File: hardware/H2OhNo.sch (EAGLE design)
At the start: 12 parts, among them U2 TINY85-20-DIP

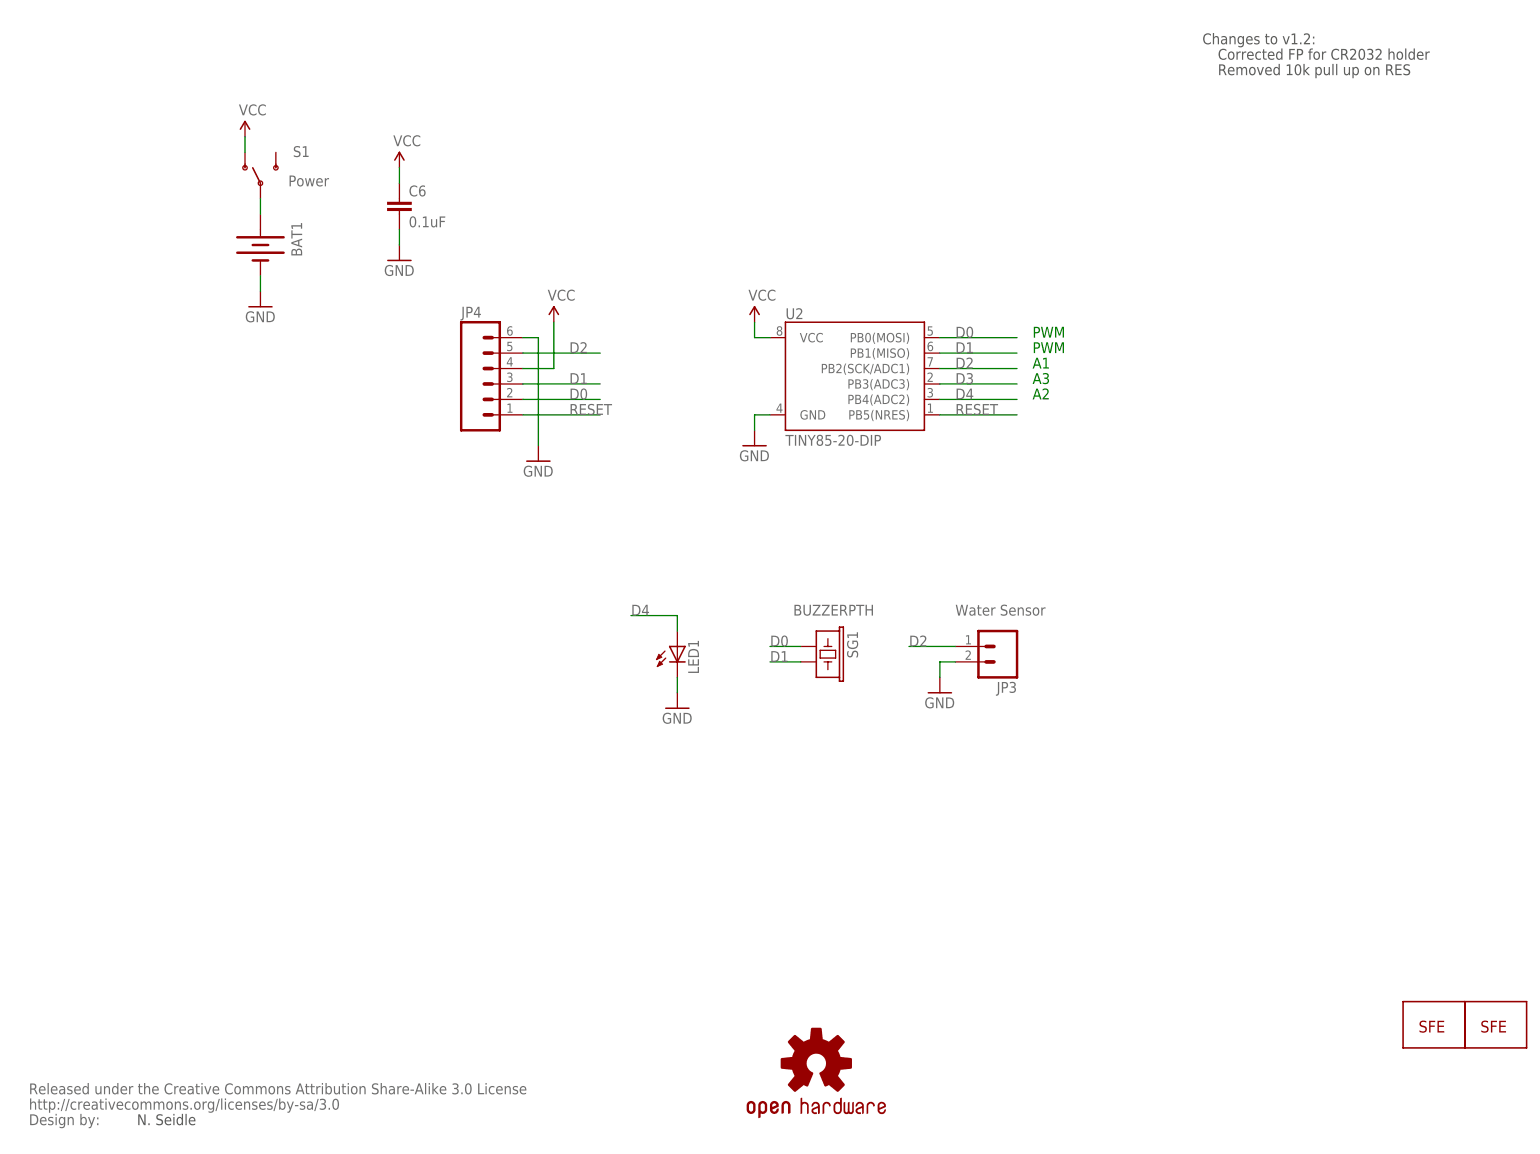
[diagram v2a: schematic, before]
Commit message: Hardware changes to address issues on github.
Moved 0.1uF cap closer to IC. Added standoffs. Increased board size.
Moved LED and sense towards end of board.
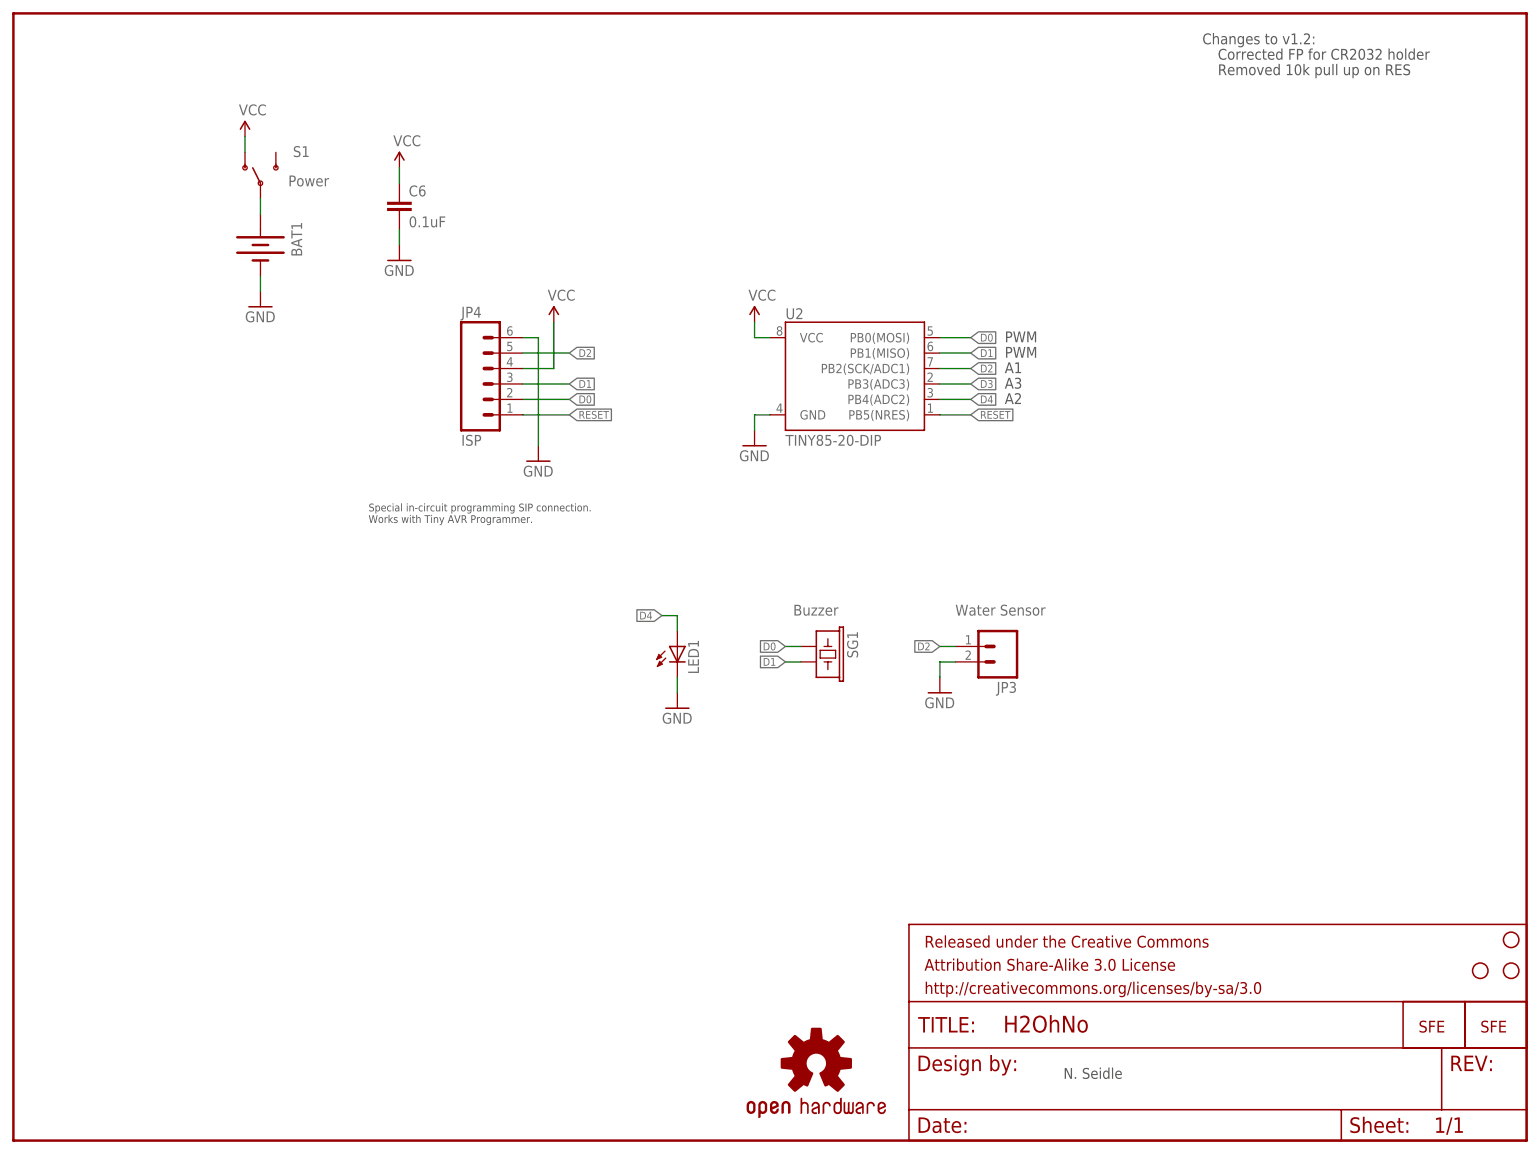
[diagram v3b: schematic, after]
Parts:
- removed U$2: CREATIVE_COMMONS, SparkFun:CREATIVE_COMMONS
- added FRAME2: FRAME-LETTER, SparkFun-Aesthetics:FRAME-LETTER
- added STANDOFF1, STANDOFF3, STANDOFF4: STAND-OFF, SparkFun-Electromechanical:STAND-OFF
- JP4: value (none) -> ISP
- SG1: value BUZZERPTH -> Buzzer
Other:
- note added: "Special in-circuit programming SIP connection. Works with Tiny AVR Programmer."

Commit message: Creating and updating example code for tutorial hook up guide.
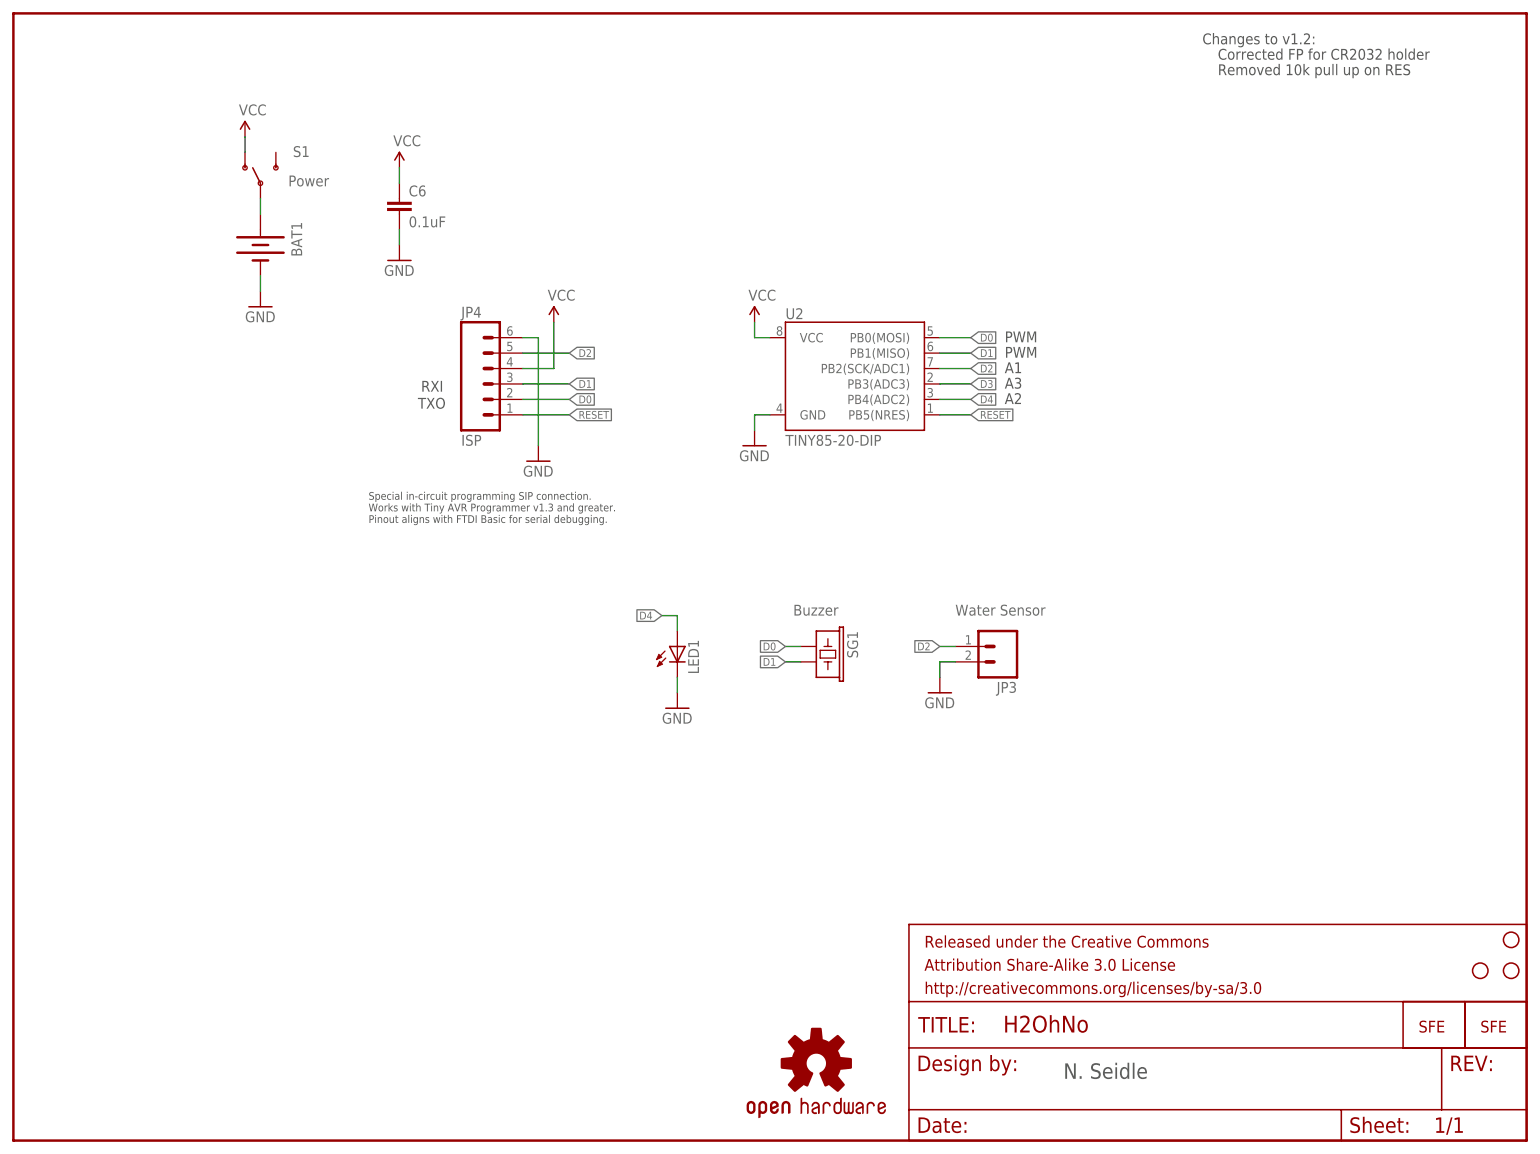
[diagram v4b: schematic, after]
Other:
- note added: "RXI"
- note added: "Special in-circuit programming SIP connection. Works with Tiny AVR Programmer v1.3 and greater. Pinout aligns with FTDI Basic for serial debugging."
- note added: "TXO"
- note removed: "Special in-circuit programming SIP connection. Works with Tiny AVR Programmer."
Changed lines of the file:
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@@
 <?xml version="1.0" encoding="utf-8"?>
 <!DOCTYPE eagle SYSTEM "eagle.dtd">
-<eagle version="6.4">
+<eagle version="6.5.0">
 <drawing>
 <settings>
@@
 <grid distance="0.1" unitdist="inch" unit="inch" style="lines" multiple="1" display="no" altdistance="0.01" altunitdist="inch" altunit="inch"/>
 <layers>
-<layer number="1" name="Top" color="4" fill="1" visible="yes" active="no"/>
-<layer number="2" name="Route2" color="1" fill="3" visible="yes" active="no"/>
-<layer number="3" name="Route3" color="4" fill="3" visible="yes" active="no"/>
-<layer number="4" name="Route4" color="1" fill="4" visible="yes" active="no"/>
-<layer number="5" name="Route5" color="4" fill="4" visible="yes" active="no"/>
-<layer number="6" name="Route6" color="1" fill="8" visible="yes" active="no"/>
-<layer number="7" name="Route7" color="4" fill="8" visible="yes" active="no"/>
-<layer number="8" name="Route8" color="1" fill="2" visible="yes" active="no"/>
-<layer number="9" name="Route9" color="4" fill="2" visible="yes" active="no"/>
-<layer number="10" name="Route10" color="1" fill="7" visible="yes" active="no"/>
-<layer number="11" name="Route11" color="4" fill="7" visible="yes" active="no"/>
-<layer number="12" name="Route12" color="1" fill="5" visible="yes" active="no"/>
-<layer number="13" name="Route13" color="4" fill="5" visible="yes" active="no"/>
-<layer number="14" name="Route14" color="1" fill="6" visible="yes" active="no"/>
-<layer number="15" name="Route15" color="4" fill="6" visible="yes" active="no"/>
-<layer number="16" name="Bottom" color="1" fill="1" visible="yes" active="no"/>
-<layer number="17" name="Pads" color="2" fill="1" visible="yes" active="no"/>
-<layer number="18" name="Vias" color="2" fill="1" visible="yes" active="no"/>
-<layer number="19" name="Unrouted" color="14" fill="1" visible="yes" active="no"/>
-<layer number="20" name="Dimension" color="15" fill="1" visible="yes" active="no"/>
-<layer number="21" name="tPlace" color="16" fill="1" visible="yes" active="no"/>
-<layer number="22" name="bPlace" color="14" fill="1" visible="yes" active="no"/>
-<layer number="23" name="tOrigins" color="15" fill="1" visible="yes" active="no"/>
-<layer number="24" name="bOrigins" color="15" fill="1" visible="yes" active="no"/>
-<layer number="25" name="tNames" color="7" fill="1" visible="yes" active="no"/>
-<layer number="26" name="bNames" color="7" fill="1" visible="yes" active="no"/>
-<layer number="27" name="tValues" color="7" fill="1" visible="yes" active="no"/>
-<layer number="28" name="bValues" color="7" fill="1" visible="yes" active="no"/>
+<layer number="1" name="Top" color="4" fill="1" visible="no" active="no"/>
+<layer number="2" name="Route2" color="1" fill="3" visible="no" active="no"/>
+<layer number="3" name="Route3" color="4" fill="3" visible="no" active="no"/>
+<layer number="4" name="Route4" color="1" fill="4" visible="no" active="no"/>
+<layer number="5" name="Route5" color="4" fill="4" visible="no" active="no"/>
+<layer number="6" name="Route6" color="1" fill="8" visible="no" active="no"/>
+<layer number="7" name="Route7" color="4" fill="8" visible="no" active="no"/>
+<layer number="8" name="Route8" color="1" fill="2" visible="no" active="no"/>
+<layer number="9" name="Route9" color="4" fill="2" visible="no" active="no"/>
+<layer number="10" name="Route10" color="1" fill="7" visible="no" active="no"/>
+<layer number="11" name="Route11" color="4" fill="7" visible="no" active="no"/>
+<layer number="12" name="Route12" color="1" fill="5" visible="no" active="no"/>
+<layer number="13" name="Route13" color="4" fill="5" visible="no" active="no"/>
+<layer number="14" name="Route14" color="1" fill="6" visible="no" active="no"/>
+<layer number="15" name="Route15" color="4" fill="6" visible="no" active="no"/>
+<layer number="16" name="Bottom" color="1" fill="1" visible="no" active="no"/>
+<layer number="17" name="Pads" color="2" fill="1" visible="no" active="no"/>
+<layer number="18" name="Vias" color="2" fill="1" visible="no" active="no"/>
+<layer number="19" name="Unrouted" color="14" fill="1" visible="no" active="no"/>
+<layer number="20" name="Dimension" color="15" fill="1" visible="no" active="no"/>
+<layer number="21" name="tPlace" color="16" fill="1" visible="no" active="no"/>
+<layer number="22" name="bPlace" color="14" fill="1" visible="no" active="no"/>
+<layer number="23" name="tOrigins" color="15" fill="1" visible="no" active="no"/>
+<layer number="24" name="bOrigins" color="15" fill="1" visible="no" active="no"/>
+<layer number="25" name="tNames" color="7" fill="1" visible="no" active="no"/>
+<layer number="26" name="bNames" color="7" fill="1" visible="no" active="no"/>
+<layer number="27" name="tValues" color="7" fill="1" visible="no" active="no"/>
+<layer number="28" name="bValues" color="7" fill="1" visible="no" active="no"/>
 <layer number="29" name="tStop" color="7" fill="3" visible="no" active="no"/>
 <layer number="30" name="bStop" color="7" fill="6" visible="no" active="no"/>
@@
 <layer number="35" name="tGlue" color="7" fill="4" visible="no" active="no"/>
 <layer number="36" name="bGlue" color="7" fill="5" visible="no" active="no"/>
-<layer number="37" name="tTest" color="7" fill="1" visible="yes" active="no"/>
-<layer number="38" name="bTest" color="7" fill="1" visible="yes" active="no"/>
+<layer number="37" name="tTest" color="7" fill="1" visible="no" active="no"/>
+<layer number="38" name="bTest" color="7" fill="1" visible="no" active="no"/>
 <layer number="39" name="tKeepout" color="4" fill="11" visible="no" active="no"/>
 <layer number="40" name="bKeepout" color="1" fill="11" visible="no" active="no"/>
@@
 <layer number="44" name="Drills" color="7" fill="1" visible="no" active="no"/>
 <layer number="45" name="Holes" color="7" fill="1" visible="no" active="no"/>
-<layer number="46" name="Milling" color="3" fill="1" visible="yes" active="no"/>
-<layer number="47" name="Measures" color="7" fill="1" visible="yes" active="no"/>
-<layer number="48" name="Document" color="7" fill="1" visible="yes" active="no"/>
-<layer number="49" name="Reference" color="7" fill="1" visible="yes" active="no"/>
-<layer number="50" name="dxf" color="7" fill="1" visible="yes" active="no"/>
-<layer number="51" name="tDocu" color="6" fill="1" visible="yes" active="no"/>
-<layer number="52" name="bDocu" color="7" fill="1" visible="yes" active="no"/>
-<layer number="53" name="tGND_GNDA" color="7" fill="9" visible="yes" active="no"/>
-<layer number="54" name="bGND_GNDA" color="1" fill="9" visible="yes" active="no"/>
-<layer number="56" name="wert" color="7" fill="1" visible="yes" active="no"/>
+<layer number="46" name="Milling" color="3" fill="1" visible="no" active="no"/>
+<layer number="47" name="Measures" color="7" fill="1" visible="no" active="no"/>
+<layer number="48" name="Document" color="7" fill="1" visible="no" active="no"/>
+<layer number="49" name="Reference" color="7" fill="1" visible="no" active="no"/>
+<layer number="50" name="dxf" color="7" fill="1" visible="no" active="no"/>
+<layer number="51" name="tDocu" color="6" fill="1" visible="no" active="no"/>
+<layer number="52" name="bDocu" color="7" fill="1" visible="no" active="no"/>
+<layer number="53" name="tGND_GNDA" color="7" fill="9" visible="no" active="no"/>
+<layer number="54" name="bGND_GNDA" color="1" fill="9" visible="no" active="no"/>
+<layer number="56" name="wert" color="7" fill="1" visible="no" active="no"/>
 <layer number="91" name="Nets" color="2" fill="1" visible="yes" active="yes"/>
 <layer number="92" name="Busses" color="1" fill="1" visible="yes" active="yes"/>
@@
 <sheet>
 <plain>
-<text x="172.72" y="10.16" size="1.778" layer="97">N. Seidle</text>
+<text x="172.72" y="10.16" size="2.54" layer="97">N. Seidle</text>
 <text x="195.58" y="180.34" size="1.778" layer="97">Changes to v1.2:</text>
 <text x="163.068" y="131.318" size="1.778" layer="97">PWM</text>
@@
 <text x="198.12" y="175.26" size="1.778" layer="97">Removed 10k pull up on RES</text>
 <text x="58.42" y="101.6" size="1.27" layer="97">Special in-circuit programming SIP connection.
-Works with Tiny AVR Programmer.</text>
+Works with Tiny AVR Programmer v1.3 and greater.
+Pinout aligns with FTDI Basic for serial debugging.</text>
+<text x="66.548" y="120.396" size="1.778" layer="97">TXO</text>
+<text x="67.056" y="123.19" size="1.778" layer="97">RXI</text>
 </plain>
 <instances>

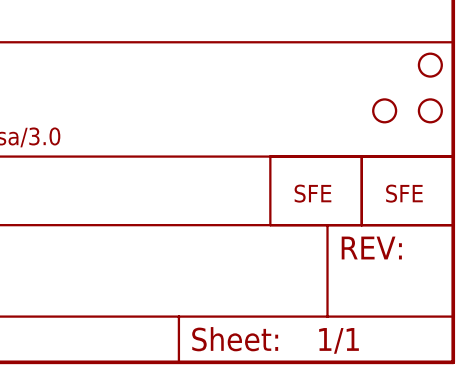
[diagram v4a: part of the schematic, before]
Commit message: Adding version number to schematic
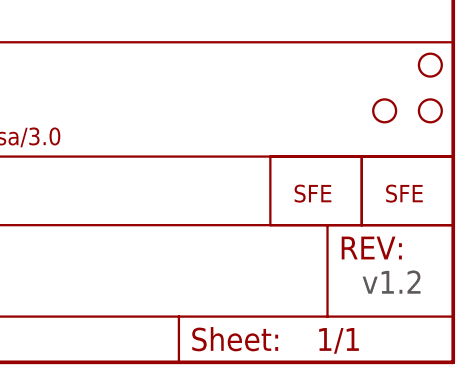
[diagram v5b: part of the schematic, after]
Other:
- note added: "v1.2"
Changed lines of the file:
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@@
 <?xml version="1.0" encoding="utf-8"?>
 <!DOCTYPE eagle SYSTEM "eagle.dtd">
-<eagle version="6.5.0">
+<eagle version="6.4">
 <drawing>
 <settings>
@@
 <text x="66.548" y="120.396" size="1.778" layer="97">TXO</text>
 <text x="67.056" y="123.19" size="1.778" layer="97">RXI</text>
+<text x="238.76" y="7.62" size="2.54" layer="97">v1.2</text>
 </plain>
 <instances>
